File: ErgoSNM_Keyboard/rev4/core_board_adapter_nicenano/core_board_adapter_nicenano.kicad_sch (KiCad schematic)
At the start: 12 parts, among them J1 Conn_01x13, J2 Conn_01x03, J3 Conn_01x13, J4 Conn_01x30, J5 Conn_Batt, SW1 SW_DPDT_x2

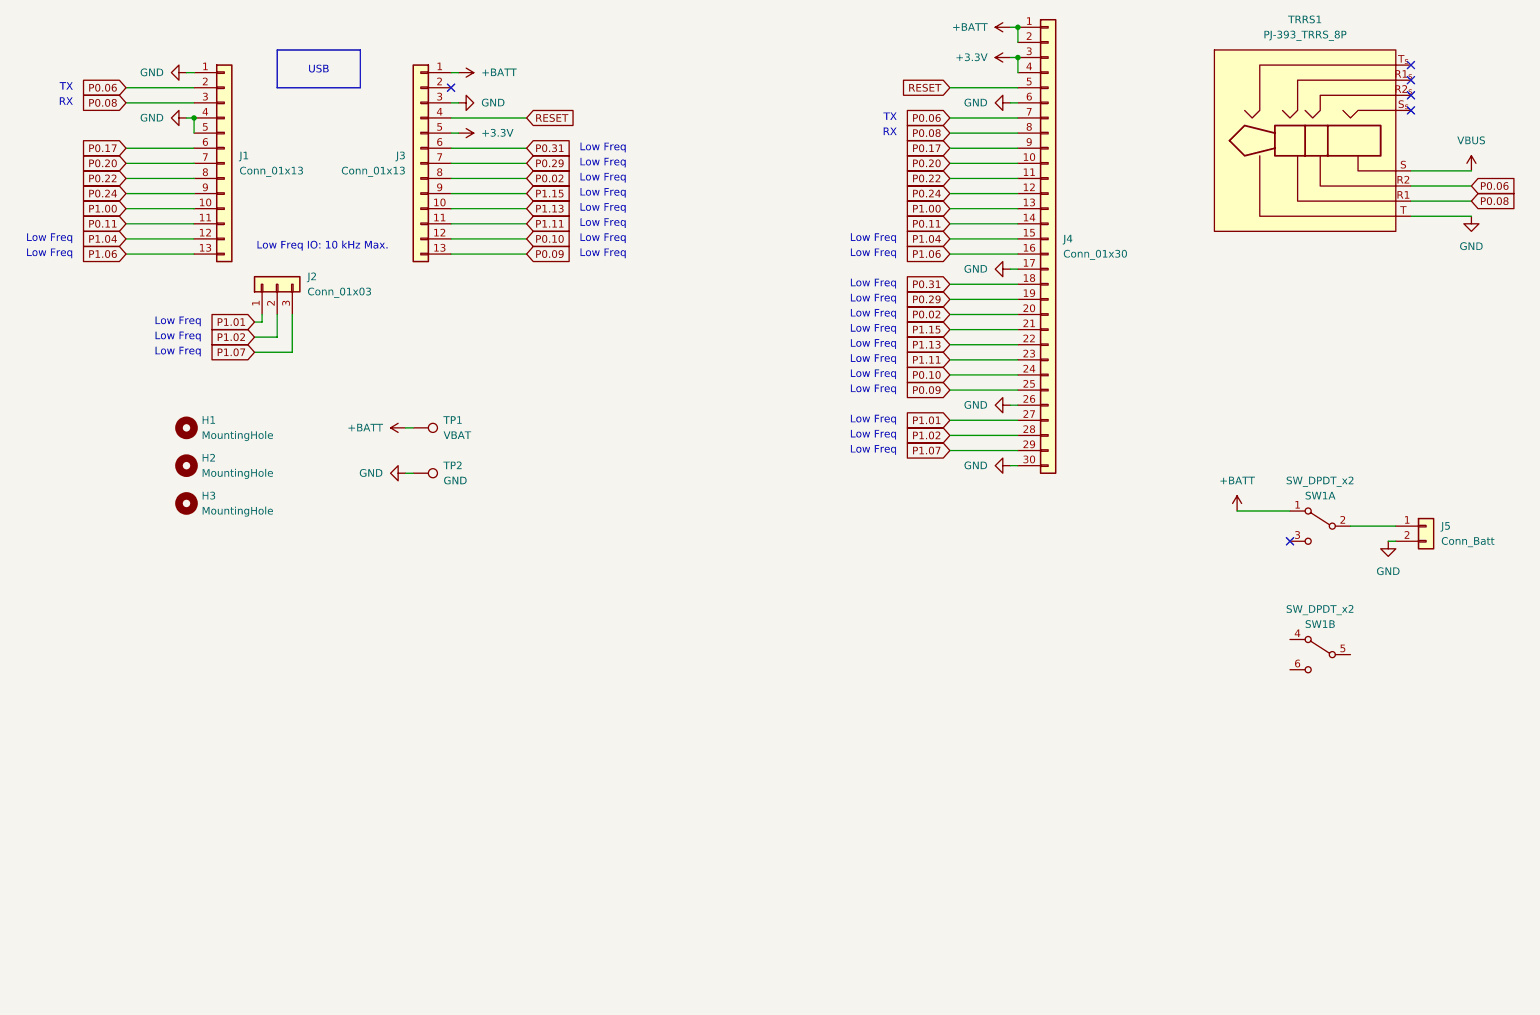
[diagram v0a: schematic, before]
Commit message: feat: update nice!nano core board
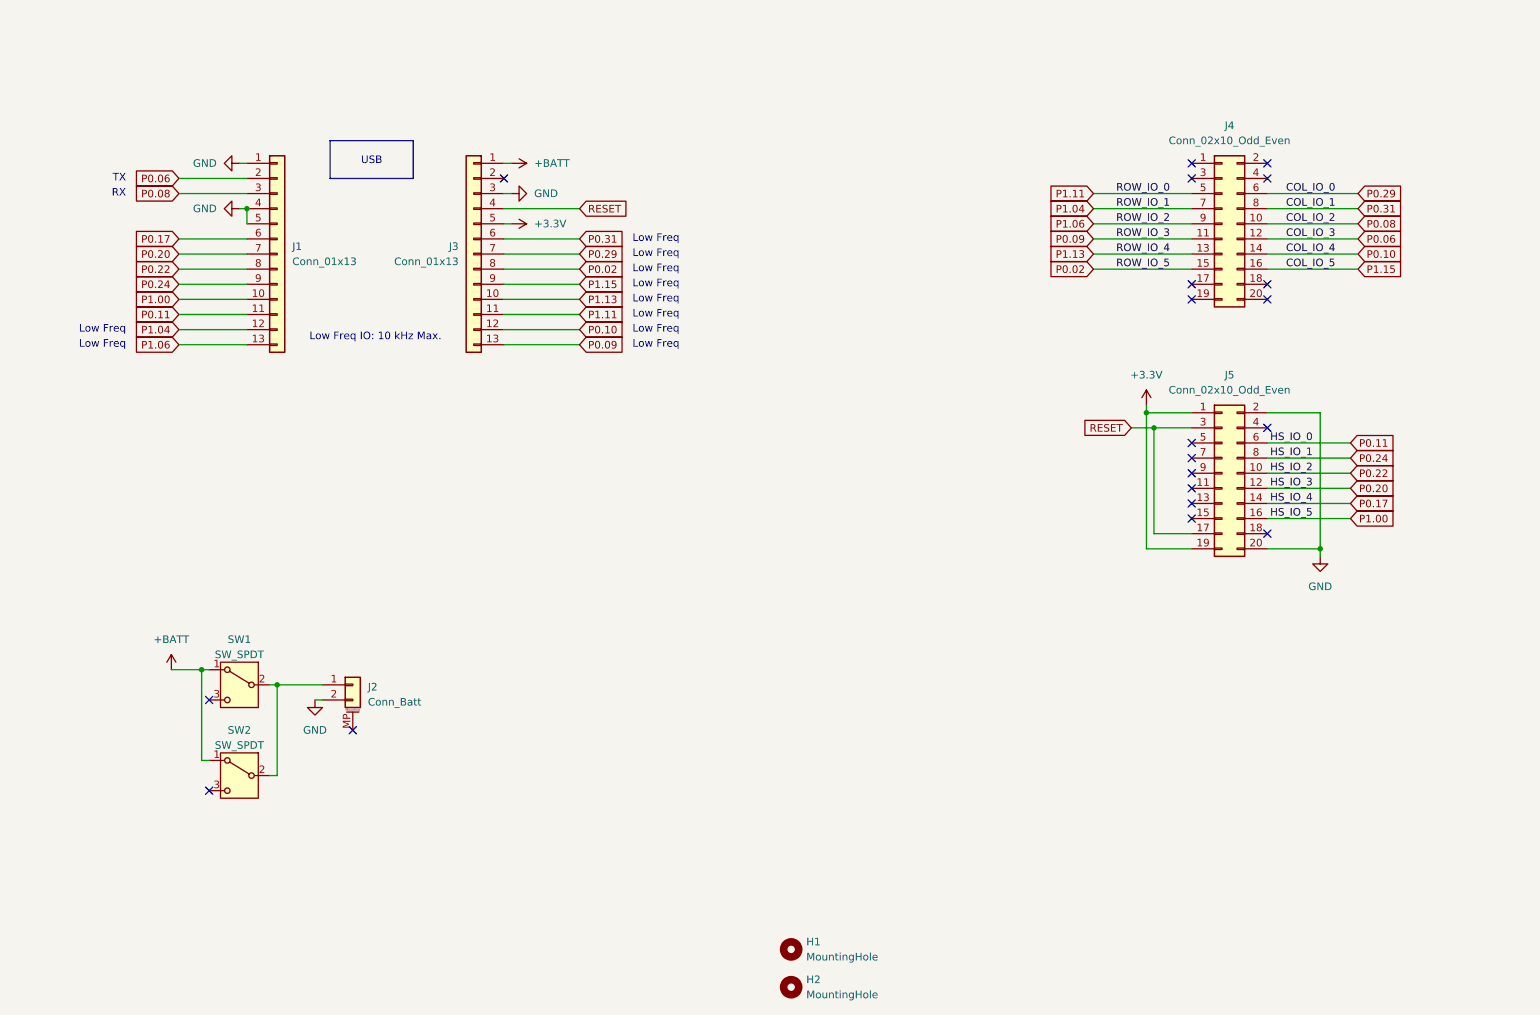
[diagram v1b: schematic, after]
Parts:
- removed H3: MountingHole, MountingHole:MountingHole_2.7mm_M2.5_ISO7380, symbol Mechanical:MountingHole
- removed J2: Conn_01x03, Connector_PinHeader_2.54mm:PinHeader_1x03_P2.54mm_Vertical, symbol Connector_Generic:Conn_01x03
- removed J4: Conn_01x30, Connector_FFC-FPC:TE_3-1734839-0_1x30-1MP_P0.5mm_Horizontal, symbol Connector_Generic:Conn_01x30
- removed J5: Conn_Batt, Connector_JST:JST_PH_S2B-PH-SM4-TB_1x02-1MP_P2.00mm_Horizontal, symbol Connector_Generic:Conn_01x02
- removed SW1: SW_DPDT_x2, ErgoSNM_Keyboard:MSKT-22D14-T, symbol Switch:SW_DPDT_x2
- removed TP1: VBAT, TestPoint:TestPoint_Keystone_5015_Micro_Mini, symbol Connector:TestPoint
- removed TP2: GND, TestPoint:TestPoint_Keystone_5015_Micro_Mini, symbol Connector:TestPoint
- removed TRRS1: PJ-393_TRRS_8P, ErgoSNM_Keyboard:PJ-393 8P TRRS, symbol ErgoSNM_Keyboard_Library:PJ-393_TRRS_8P
- added J2: Conn_Batt, Connector_JST:JST_PH_S2B-PH-SM4-TB_1x02-1MP_P2.00mm_Horizontal, symbol Connector_Generic_MountingPin:Conn_01x02_MountingPin
- added J4, J5: Conn_02x10_Odd_Even, Connector_PinHeader_1.27mm:PinHeader_2x10_P1.27mm_Vertical, symbol Connector_Generic:Conn_02x10_Odd_Even
- added SW1, SW2: SW_SPDT, ErgoSNM_Keyboard:9_3.5_3.5_switch, symbol Switch:SW_SPDT
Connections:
- net +3.3V: now also J5.1 (Pin_1), J5.19 (Pin_19)
- net +BATT: now also SW1.1 (A), SW2.1 (A)
- net GND: now also J2.2 (Pin_2), J5.2 (Pin_2), J5.20 (Pin_20)
- net P0.02: now also J4.15 (Pin_15)
- net P0.06: now also J4.12 (Pin_12)
- net P0.08: now also J4.10 (Pin_10)
- net P0.09: now also J4.11 (Pin_11)
- net P0.10: now also J4.14 (Pin_14)
- net P0.11: now also J5.6 (Pin_6)
- net P0.17: now also J5.14 (Pin_14)
- net P0.20: now also J5.12 (Pin_12)
- net P0.22: now also J5.10 (Pin_10)
- net P0.24: now also J5.8 (Pin_8)
- net P0.29: now also J4.6 (Pin_6)
- net P0.31: now also J4.8 (Pin_8)
- net P1.00: now also J5.16 (Pin_16)
- net P1.04: now also J4.7 (Pin_7)
- net P1.06: now also J4.9 (Pin_9)
- net P1.11: now also J4.5 (Pin_5)
- net P1.13: now also J4.13 (Pin_13)
- net P1.15: now also J4.16 (Pin_16)
- net RESET: now also J5.17 (Pin_17), J5.3 (Pin_3)
- new net: J2.1 (Pin_1), SW1.2 (B), SW2.2 (B)
- no-connect marks 6 -> 20
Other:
- moved on the sheet: H1, H2, J1, J3
